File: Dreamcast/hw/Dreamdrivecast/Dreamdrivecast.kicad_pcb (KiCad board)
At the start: 2 copper layers, 88.9 x 77.2 mm, 9 parts, among them CN1 Molex_52602_0579, J1 Breakout, J2 POWER, J4 Micro_SD_Card, SW1 Lid, U1 WeAct-RP2040-Pico, U2 WeAct-RP2040-Pico

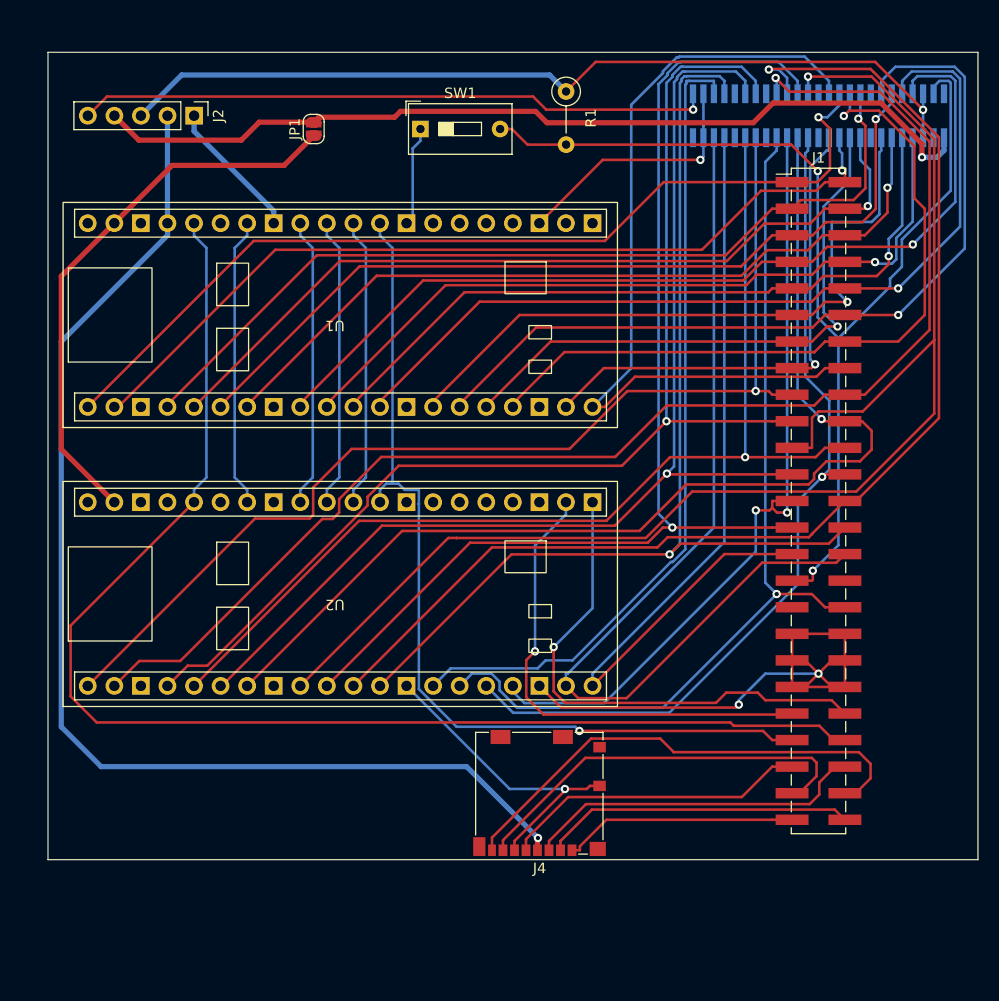
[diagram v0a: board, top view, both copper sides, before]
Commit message: Routed board, did copper fill, added silk screen for breakout, added logo and board text. Ready for fab
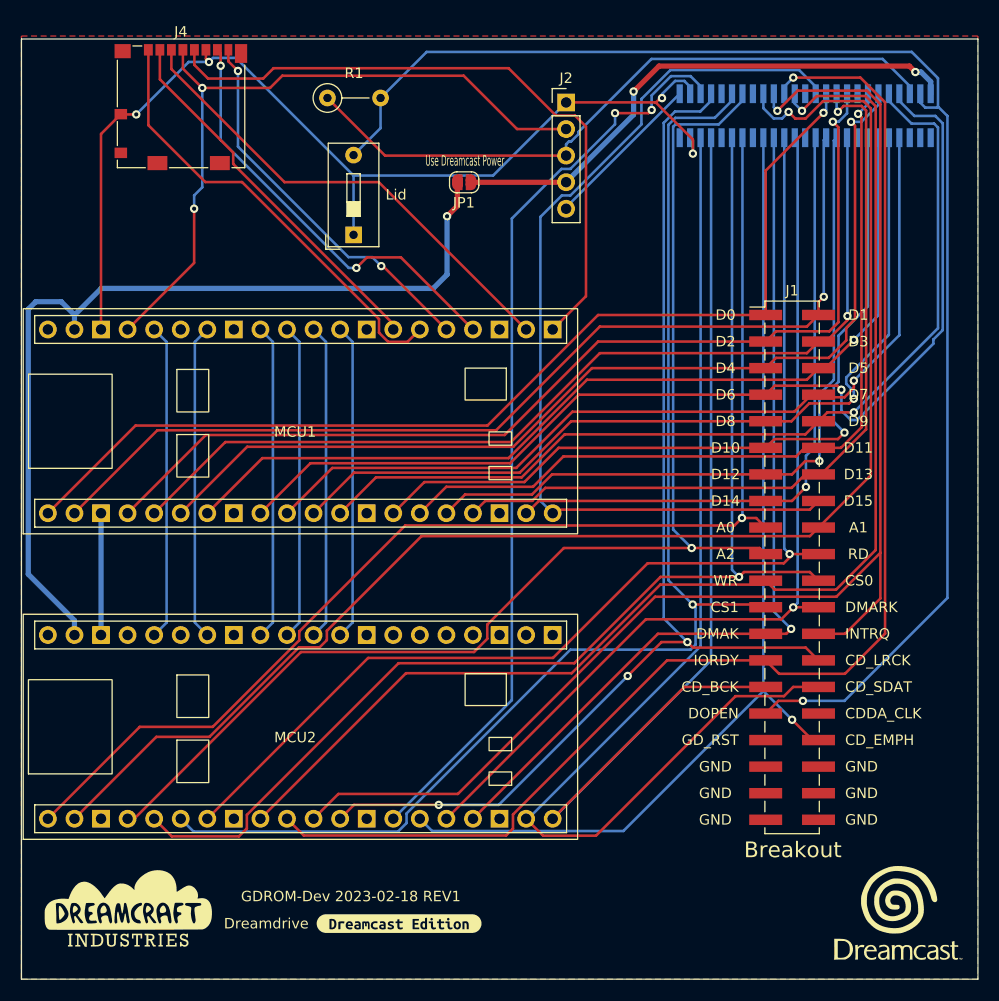
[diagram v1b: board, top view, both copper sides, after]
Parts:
- added G***: LOGO, LOGO, F.Cu at (190.5, 129.5)
- added G***: LOGO, LOGO, F.Cu at (116.8, 129.5)
- added kibuzzard-63F149CE: G***, kibuzzard-63F149CE, F.Cu at (142.8, 130.6)
- J1: footprint Connector_PinHeader_2.54mm:PinHeader_2x25_P2.54mm_Vertical_SMD -> Connector_PinHeader_2.54mm:PinHeader_2x20_P2.54mm_Vertical_SMD
- moved J4 74.0 mm to (121.9, 52.5), turned to 0 degrees
- moved J2 35.6 mm to (158.8, 52.1), turned to 0 degrees
- moved R1 22.8 mm to (135.9, 51.6), turned to 0 degrees
- moved JP1 15.3 mm to (149.0, 59.7), turned to 0 degrees
- moved MCU2 13.3 mm to (133.3, 111.8)
- moved SW1 12.0 mm to (138.4, 64.7), turned to 90 degrees
- moved MCU1 10.9 mm to (133.3, 82.5)
- moved J1 6.83 mm to (180.4, 96.5)
- moved CN1 1.27 mm to (181.6, 53.3)
- renumbered U1 to MCU1, U2 to MCU2
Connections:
- CN1 pad A1: +3V3 -> unconnected-(CN1-PadA1)
- CN1 pad A13: GND -> unconnected-(CN1-PadA13)
- CN1 pad A18: GND -> unconnected-(CN1-PadA18)
- CN1 pad A21: GND -> unconnected-(CN1-PadA21)
- CN1 pad A25: +12V -> unconnected-(CN1-PadA25)
- CN1 pad A3: +5V -> unconnected-(CN1-PadA3)
- CN1 pad A8: GND -> unconnected-(CN1-PadA8)
- CN1 pad B13: GND -> unconnected-(CN1-PadB13)
- CN1 pad B18: GND -> unconnected-(CN1-PadB18)
- CN1 pad B21: GND -> unconnected-(CN1-PadB21)
- CN1 pad B8: GND -> unconnected-(CN1-PadB8)
- J4 pad 1: /SD_DAT2 -> /SD_PIO_2
- J4 pad 3: /SD_CMD -> /SD_PIO_CMD
- J4 pad 5: /SD_CLK -> /SD_PIO_CLK
- J4 pad 8: /SD_DAT1 -> /SD_PIO_1
- MCU1 pad 13: unconnected-(U1-Pad13) -> GND
- MCU1 pad 18: unconnected-(U1-Pad13) -> unconnected-(U1-Pad18)
- MCU1 pad 24: /SD_PIO_0 -> /SD_DAT0
- MCU1 pad 27: /SD_PIO_3 -> /SD_DAT3
- MCU1 pad 3: unconnected-(U1-Pad13) -> GND
- MCU1 pad 8: unconnected-(U1-Pad13) -> GND
- MCU2 pad 13: GND -> unconnected-(U2-Pad13)
- MCU2 pad 18: GND -> unconnected-(U2-Pad18)
- MCU2 pad 28: unconnected-(U2-Pad23) -> unconnected-(U2-Pad28)
- MCU2 pad 33: unconnected-(U2-Pad23) -> unconnected-(U2-Pad33)
- MCU2 pad 38: unconnected-(U2-Pad23) -> GND
- MCU2 pad 8: GND -> unconnected-(U2-Pad8)
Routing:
- net /MCU_CTRL1: track 126.9 -> 30.2 mm
- net /SD_PIO_CLK: track 0.00 -> 62.9 mm
- net /MCU_CTRL0: track 87.5 -> 30.2 mm, vias 1 -> 0
- net /MCU2_UART_TX: track 49.2 -> 0.00 mm, vias 1 -> 0
- net /SD_DAT1: track 46.7 -> 0.00 mm
- net /MCU2_UART_RX: track 46.4 -> 0.00 mm, vias 1 -> 0
- net /SD_PIO_CMD: track 0.00 -> 46.1 mm
- net /PICO_3v3_OUT: track 113.8 -> 67.8 mm, vias 1 -> 2
- net +12V: track 60.7 -> 15.5 mm, vias 1 -> 0
- net /SD_PIO_2: track 0.00 -> 43.0 mm
- net /SD_PIO_1: track 0.00 -> 36.8 mm, vias 0 -> 2
- net +3V3: track 87.0 -> 51.7 mm, vias 1 -> 2
- net /SD_CMD: track 32.8 -> 0.00 mm
- net /PICO_VSYS: track 53.4 -> 86.1 mm, vias 0 -> 1
- net /DOPEN: track 106.4 -> 137.5 mm, vias 2 -> 1
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- added copper zone on F.Cu, net GND
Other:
- board size 88.9 x 77.2 mm -> 91.4 x 89.9 mm
- board text added: "A0"
- board text added: "A1"
- board text added: "A2"
- board text added: "CDDA_CLK"
- board text added: "CD_BCK"
- board text added: "CD_EMPH"
- board text added: "CD_LRCK"
- board text added: "CD_SDAT"
- board text added: "CS0"
- board text added: "CS1"
- board text added: "D0"
- board text added: "D1"
- board text added: "D10"
- board text added: "D11"
- board text added: "D12"
- board text added: "D13"
- board text added: "D14"
- board text added: "D15"
- board text added: "D2"
- board text added: "D3"
- board text added: "D4"
- board text added: "D5"
- board text added: "D6"
- board text added: "D7"
- board text added: "D8"
- board text added: "D9"
- board text added: "DMAK"
- board text added: "DMARK"
- board text added: "DOPEN"
- board text added: "Dreamdrive"
- board text added: "GDROM-Dev 2023-02-18 REV1"
- board text added: "GD_RST"
- board text added: "GND"
- board text added: "INTRQ"
- board text added: "IORDY"
- board text added: "RD"
- board text added: "WR"
